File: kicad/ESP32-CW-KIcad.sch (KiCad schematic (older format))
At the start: 21 parts, among them Q1 BS170, Q2 IRFU9024, Q3 BS170, Q4 BS170, Q5 BS170, SW1 SW_Push, U1 LD33V, U2 L7805, U3 7402, U4 si5351, U5 ESP32-15-PIN

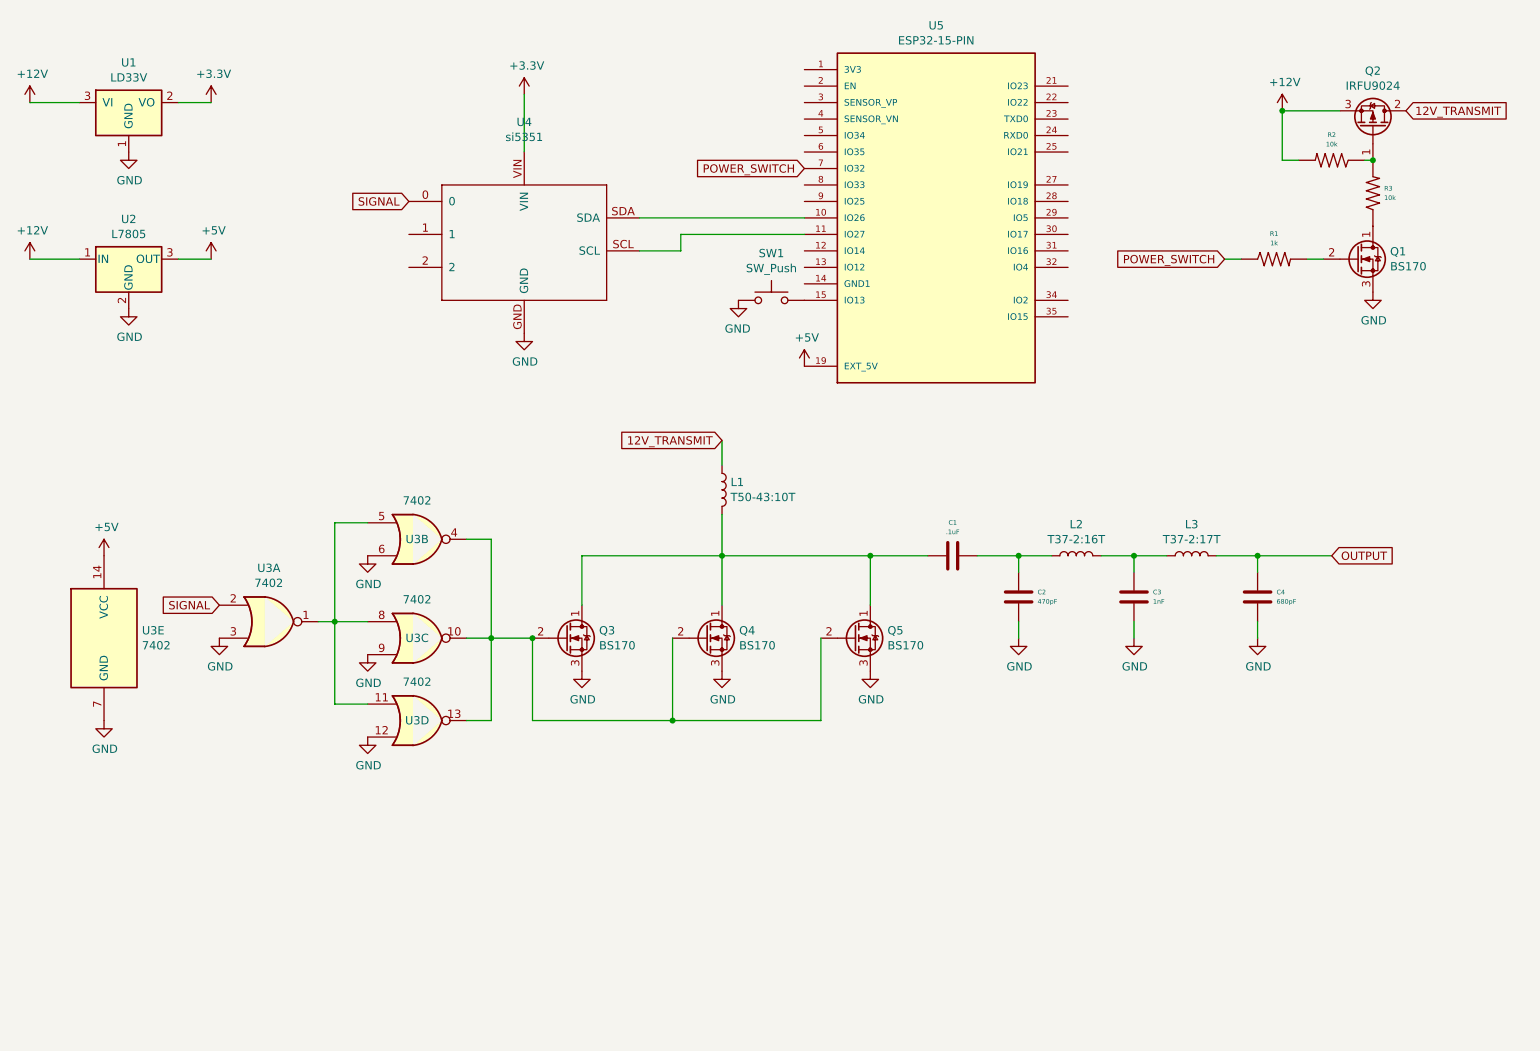
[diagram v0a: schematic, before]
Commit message: added lm386
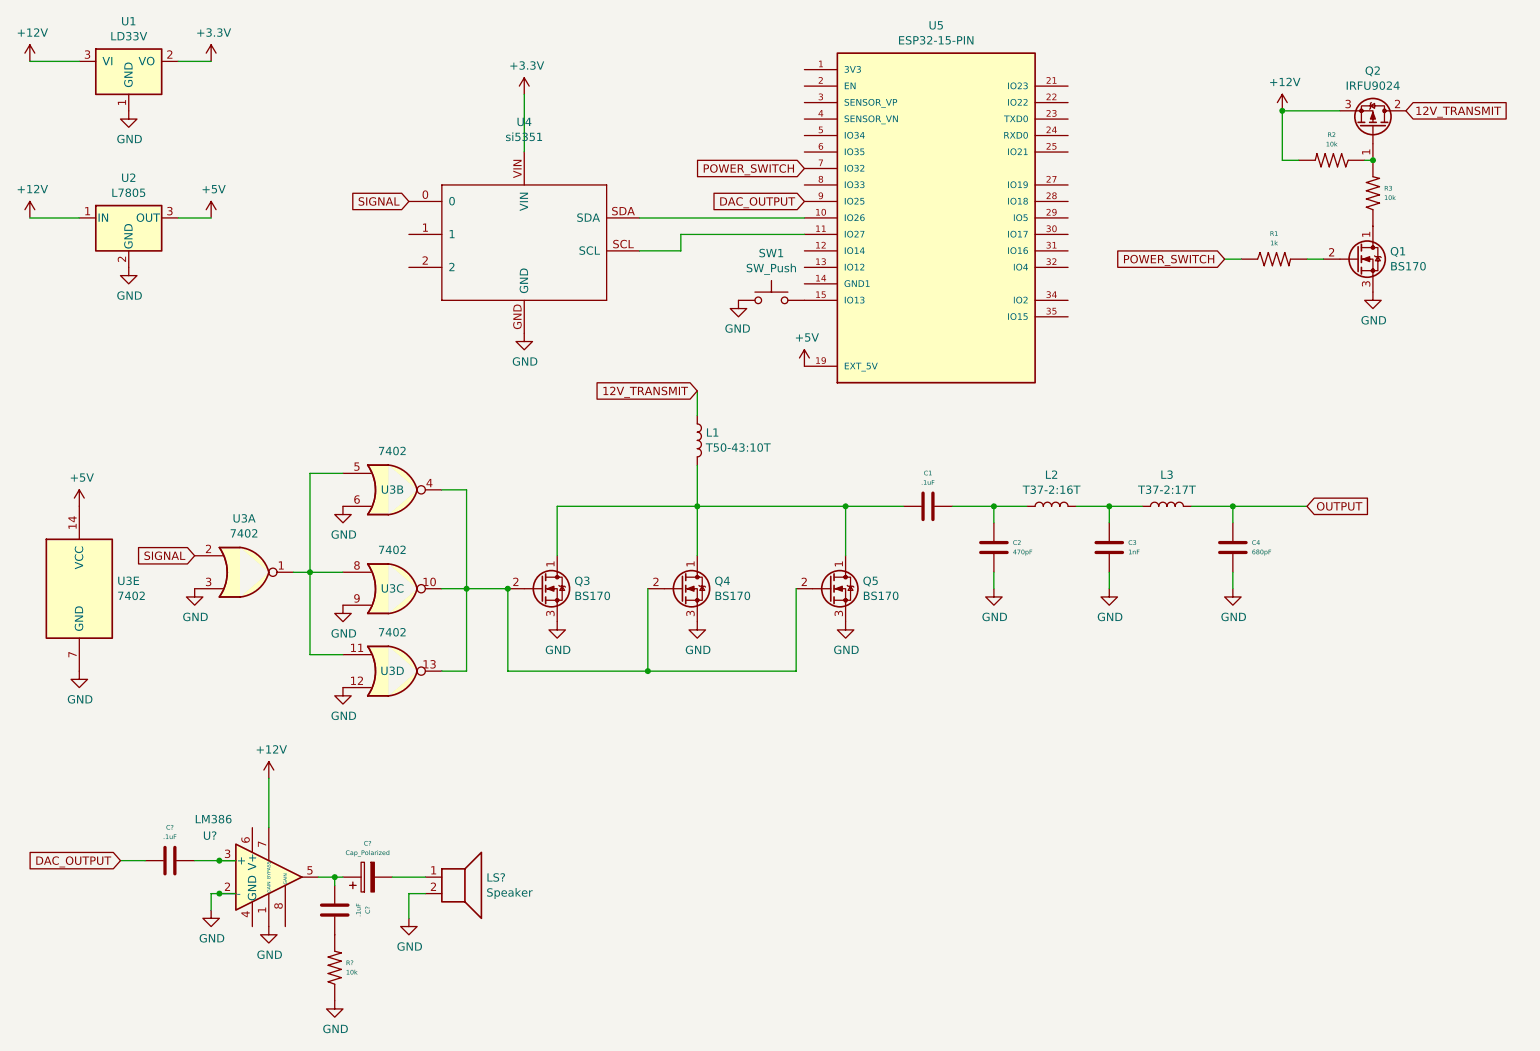
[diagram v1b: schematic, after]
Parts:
- added C? (x2): .1uF, symbol Xenir:Capacitor
- added C?: Cap_Polarized, symbol Xenir:Cap_Polarized
- added LS?: Speaker, symbol Device:Speaker
- added R?: 10k, symbol Xenir:Resistor
- added U?: LM386, symbol Amplifier_Audio:LM386
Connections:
- net labels added: DAC_OUTPUT
- wire segments 52 -> 65
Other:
- moved on the sheet: C1, C2, C3, C4, L1, L2, L3, Q3, Q4, Q5, U1, U2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
